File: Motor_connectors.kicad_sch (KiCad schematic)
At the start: 3 parts

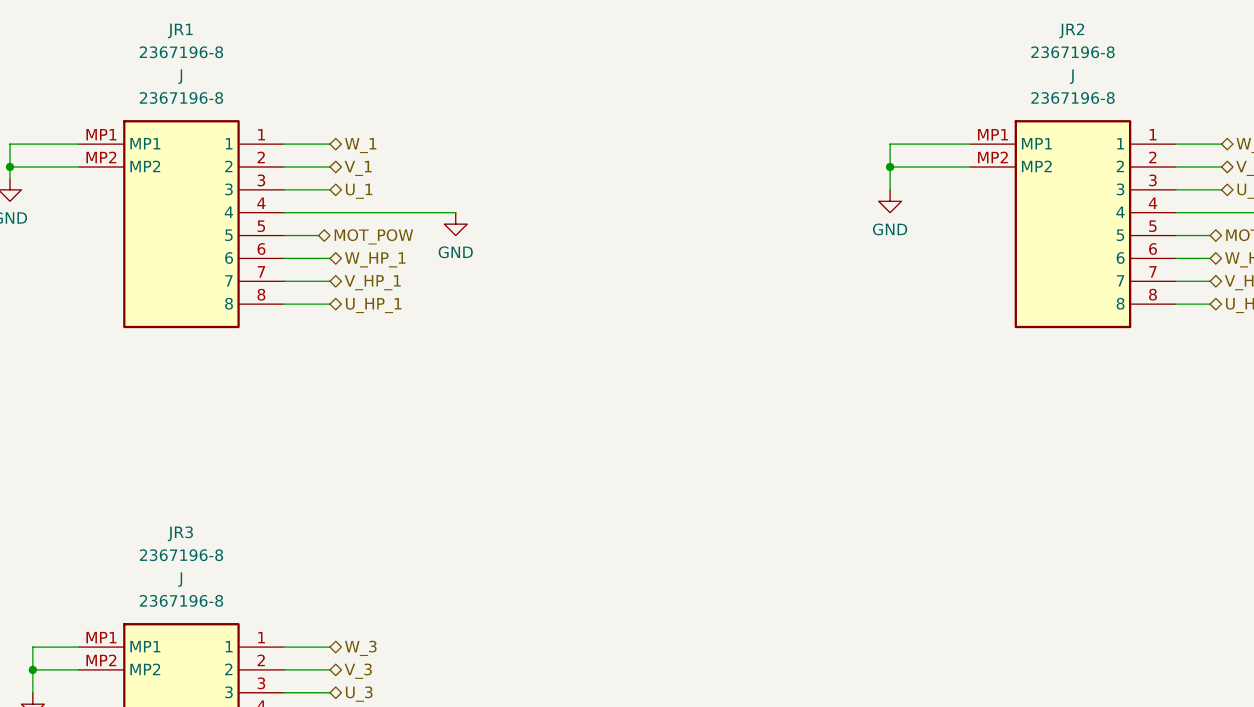
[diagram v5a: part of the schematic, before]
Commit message: Page settings changed. Added some testpoints. Some comments are made.
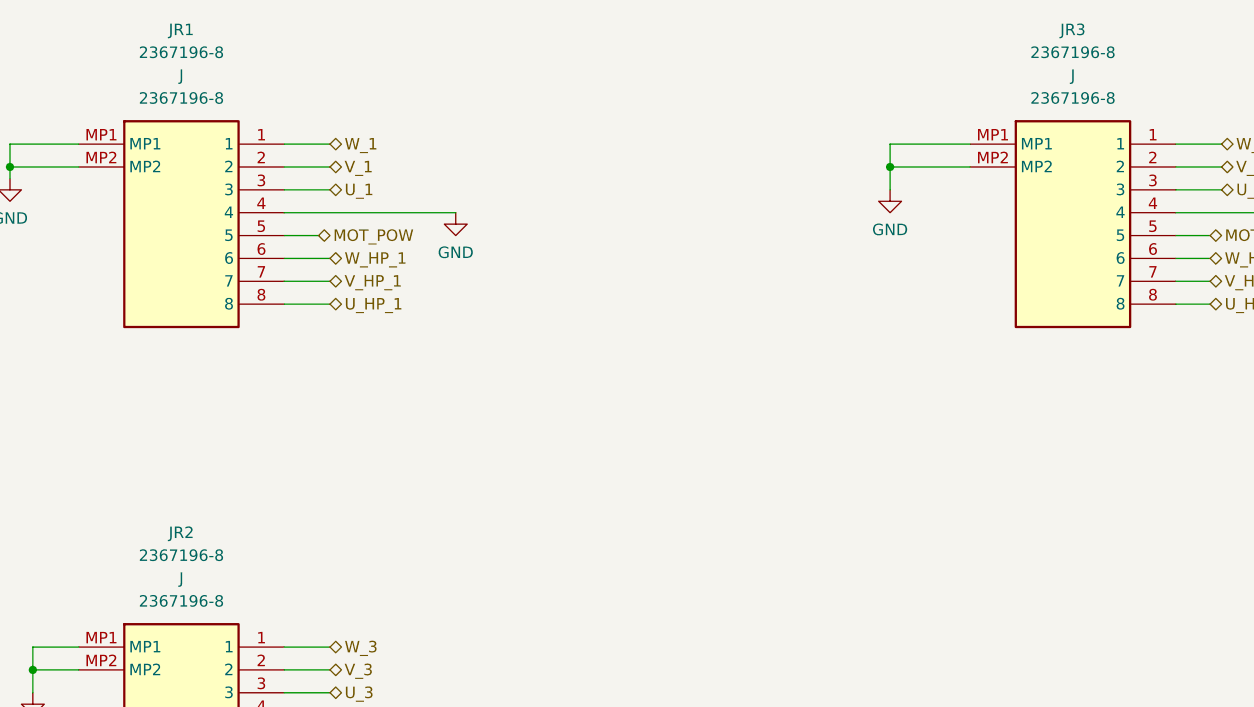
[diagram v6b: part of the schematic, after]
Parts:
- renumbered JR3 to JR2, JR2 to JR3
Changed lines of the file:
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@@
   (symbol (lib_id "upsat-comms-hardware:GND") (at 133.35 58.42 0) (unit 1)
     (in_bom yes) (on_board yes) (fields_autoplaced)
-    (property "Reference" "#PWR098" (id 0) (at 133.35 64.77 0)
+    (property "Reference" "#PWR0114" (id 0) (at 133.35 64.77 0)
       (effects (font (size 1.27 1.27)) hide)
     )
@@
   (symbol (lib_id "upsat-comms-hardware:GND") (at 85.09 60.96 0) (unit 1)
     (in_bom yes) (on_board yes) (fields_autoplaced)
-    (property "Reference" "#PWR099" (id 0) (at 85.09 67.31 0)
+    (property "Reference" "#PWR0112" (id 0) (at 85.09 67.31 0)
       (effects (font (size 1.27 1.27)) hide)
     )
@@
   (symbol (lib_id "upsat-comms-hardware:GND") (at 181.61 60.96 0) (unit 1)
     (in_bom yes) (on_board yes) (fields_autoplaced)
-    (property "Reference" "#PWR0100" (id 0) (at 181.61 67.31 0)
+    (property "Reference" "#PWR0115" (id 0) (at 181.61 67.31 0)
       (effects (font (size 1.27 1.27)) hide)
     )
@@
   (symbol (lib_id "upsat-comms-hardware:GND") (at 35.56 57.15 0) (unit 1)
     (in_bom yes) (on_board yes) (fields_autoplaced)
-    (property "Reference" "#PWR097" (id 0) (at 35.56 63.5 0)
+    (property "Reference" "#PWR0110" (id 0) (at 35.56 63.5 0)
       (effects (font (size 1.27 1.27)) hide)
     )
@@
   (symbol (lib_id "2367196-8:2367196-8") (at 43.18 109.22 0) (unit 1)
     (in_bom yes) (on_board yes) (fields_autoplaced)
-    (property "Reference" "JR3" (id 0) (at 54.61 96.52 0))
+    (property "Reference" "JR2" (id 0) (at 54.61 96.52 0))
     (property "Value" "2367196-8" (id 1) (at 54.61 99.06 0))
     (property "Footprint" "" (id 2) (at 43.18 109.22 0)
@@
   (symbol (lib_id "upsat-comms-hardware:GND") (at 86.36 116.84 0) (unit 1)
     (in_bom yes) (on_board yes) (fields_autoplaced)
-    (property "Reference" "#PWR0102" (id 0) (at 86.36 123.19 0)
+    (property "Reference" "#PWR0113" (id 0) (at 86.36 123.19 0)
       (effects (font (size 1.27 1.27)) hide)
     )
@@
   (symbol (lib_id "2367196-8:2367196-8") (at 142.24 53.34 0) (unit 1)
     (in_bom yes) (on_board yes) (fields_autoplaced)
-    (property "Reference" "JR2" (id 0) (at 153.67 40.64 0))
+    (property "Reference" "JR3" (id 0) (at 153.67 40.64 0))
     (property "Value" "2367196-8" (id 1) (at 153.67 43.18 0))
     (property "Footprint" "" (id 2) (at 142.24 53.34 0)
@@
   (symbol (lib_id "upsat-comms-hardware:GND") (at 38.1 114.3 0) (unit 1)
     (in_bom yes) (on_board yes) (fields_autoplaced)
-    (property "Reference" "#PWR0101" (id 0) (at 38.1 120.65 0)
+    (property "Reference" "#PWR0111" (id 0) (at 38.1 120.65 0)
       (effects (font (size 1.27 1.27)) hide)
     )

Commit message: I2C lines are pulled up
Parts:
- JR1, JR2, JR3: footprint (none) -> 2367196-8:23671968
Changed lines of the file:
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@@
     (property "Reference" "JR1" (id 0) (at 54.61 40.64 0))
     (property "Value" "2367196-8" (id 1) (at 54.61 43.18 0))
-    (property "Footprint" "" (id 2) (at 43.18 53.34 0)
+    (property "Footprint" "2367196-8:23671968" (id 2) (at 43.18 53.34 0)
       (effects (font (size 1.27 1.27)) hide)
     )
@@
   (symbol (lib_id "upsat-comms-hardware:GND") (at 133.35 58.42 0) (unit 1)
     (in_bom yes) (on_board yes) (fields_autoplaced)
-    (property "Reference" "#PWR0114" (id 0) (at 133.35 64.77 0)
+    (property "Reference" "#PWR0115" (id 0) (at 133.35 64.77 0)
       (effects (font (size 1.27 1.27)) hide)
     )
@@
   (symbol (lib_id "upsat-comms-hardware:GND") (at 85.09 60.96 0) (unit 1)
     (in_bom yes) (on_board yes) (fields_autoplaced)
-    (property "Reference" "#PWR0112" (id 0) (at 85.09 67.31 0)
+    (property "Reference" "#PWR0113" (id 0) (at 85.09 67.31 0)
       (effects (font (size 1.27 1.27)) hide)
     )
@@
   (symbol (lib_id "upsat-comms-hardware:GND") (at 181.61 60.96 0) (unit 1)
     (in_bom yes) (on_board yes) (fields_autoplaced)
-    (property "Reference" "#PWR0115" (id 0) (at 181.61 67.31 0)
+    (property "Reference" "#PWR0116" (id 0) (at 181.61 67.31 0)
       (effects (font (size 1.27 1.27)) hide)
     )
@@
   (symbol (lib_id "upsat-comms-hardware:GND") (at 35.56 57.15 0) (unit 1)
     (in_bom yes) (on_board yes) (fields_autoplaced)
-    (property "Reference" "#PWR0110" (id 0) (at 35.56 63.5 0)
+    (property "Reference" "#PWR0111" (id 0) (at 35.56 63.5 0)
       (effects (font (size 1.27 1.27)) hide)
     )
@@
     (property "Reference" "JR2" (id 0) (at 54.61 96.52 0))
     (property "Value" "2367196-8" (id 1) (at 54.61 99.06 0))
-    (property "Footprint" "" (id 2) (at 43.18 109.22 0)
+    (property "Footprint" "2367196-8:23671968" (id 2) (at 43.18 109.22 0)
       (effects (font (size 1.27 1.27)) hide)
     )
@@
   (symbol (lib_id "upsat-comms-hardware:GND") (at 86.36 116.84 0) (unit 1)
     (in_bom yes) (on_board yes) (fields_autoplaced)
-    (property "Reference" "#PWR0113" (id 0) (at 86.36 123.19 0)
+    (property "Reference" "#PWR0114" (id 0) (at 86.36 123.19 0)
       (effects (font (size 1.27 1.27)) hide)
     )
@@
     (property "Reference" "JR3" (id 0) (at 153.67 40.64 0))
     (property "Value" "2367196-8" (id 1) (at 153.67 43.18 0))
-    (property "Footprint" "" (id 2) (at 142.24 53.34 0)
+    (property "Footprint" "2367196-8:23671968" (id 2) (at 142.24 53.34 0)
       (effects (font (size 1.27 1.27)) hide)
     )
@@
   (symbol (lib_id "upsat-comms-hardware:GND") (at 38.1 114.3 0) (unit 1)
     (in_bom yes) (on_board yes) (fields_autoplaced)
-    (property "Reference" "#PWR0111" (id 0) (at 38.1 120.65 0)
+    (property "Reference" "#PWR0112" (id 0) (at 38.1 120.65 0)
       (effects (font (size 1.27 1.27)) hide)
     )

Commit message: Final Schematic
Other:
- moved on the sheet: JR1, JR2, JR3
